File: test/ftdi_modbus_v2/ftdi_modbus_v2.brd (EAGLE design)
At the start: 50 x 50 mm, 31 parts, among them IC1 SP483E, IC2 FT232RL, J1 MB_CONN, J2 CLIFF_DCJACK2.1-2.5MM

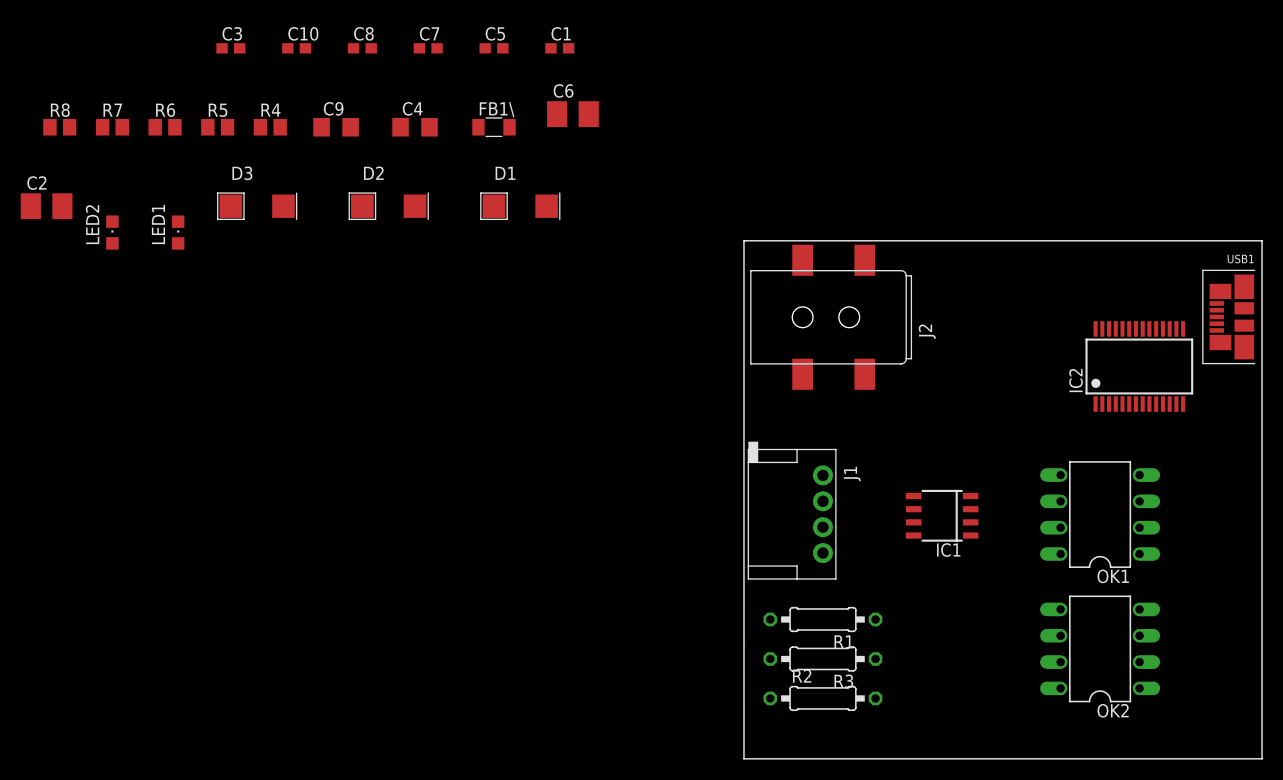
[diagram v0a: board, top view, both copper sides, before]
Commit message: Completed layout of ftdi_rs485_v2 test board. Added more status LEDs
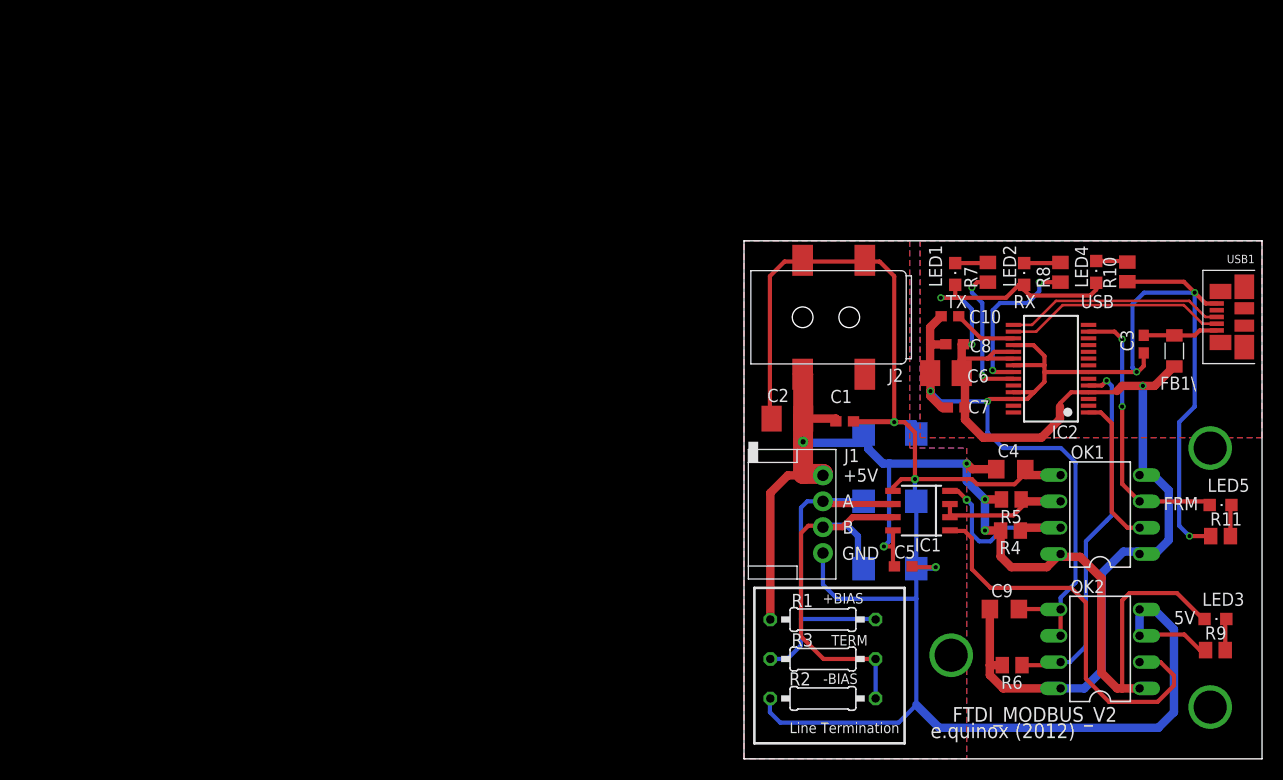
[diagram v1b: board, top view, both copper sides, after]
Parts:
- added LED3, LED4, LED5: AMBER, led:CHIPLED_0805
- added R10, R11, R9: 270, resistor:M0805
- moved R8 97.6 mm to (30.5, 47.0), turned to 90 degrees
- moved R6 96.9 mm to (25.9, 9.04), turned to 180 degrees
- moved C3 92.6 mm to (38.6, 40.0), turned to 270 degrees
- moved LED2 88.1 mm to (27.0, 46.8)
- moved R7 85.7 mm to (23.5, 47.0), turned to 90 degrees
- moved R5 84.6 mm to (25.8, 25.0), turned to 180 degrees
- moved R4 81.4 mm to (25.7, 22.0), turned to 180 degrees
- moved C9 79.5 mm to (25.1, 14.5)
- moved LED1 75.1 mm to (20.4, 46.8)
- moved C2 74.4 mm to (4.19, 32.8)
- moved D3 70.4 mm to (14.1, 18.4), flipped to the bottom, turned to 180 degrees
- moved FB1\ 69.1 mm to (41.5, 39.4), turned to 90 degrees
- moved C10 68.2 mm to (19.9, 42.7), turned to 180 degrees
- moved C4 66.3 mm to (25.8, 28.0)
- moved C8 63.9 mm to (20.3, 40.0), turned to 180 degrees
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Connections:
- new net N$7: LED3.C, R9.2
- new net N$8: LED4.C, R10.2
- new net N$9: LED5.C, R11.2
- net +5V/1: now also LED4.A
- net +5V/2: now also LED3.A
- net FTDI_TXEN: now also LED5.A
- net GND1: now also R10.1, R11.1
- net GND2: now also R9.1
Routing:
- net GND2: track 0.00 -> 181.2 mm, vias 0 -> 3
- net GND1: track 0.00 -> 129.4 mm, vias 0 -> 5
- net +5V/2: track 0.00 -> 123.4 mm, vias 0 -> 5
- net +5V/1: track 0.00 -> 120.9 mm, vias 0 -> 3
- net ISO_RXD: track 0.00 -> 40.2 mm
- net RS485_N: track 0.00 -> 39.2 mm
- net RS485_P: track 0.00 -> 37.2 mm
- net FTDI_RXD: track 0.00 -> 35.7 mm, vias 0 -> 1
- net FTDI_TXEN: track 0.00 -> 27.0 mm, vias 0 -> 2
- net USB_N: track 0.00 -> 21.4 mm
- net USB_P: track 0.00 -> 21.2 mm
- net ISO_TXD: track 0.00 -> 19.0 mm, vias 0 -> 1
- net RX_LED: track 0.00 -> 16.2 mm, vias 0 -> 2
- net FTDI_TXD: track 0.00 -> 14.5 mm
- net TX_LED: track 0.00 -> 14.0 mm, vias 0 -> 2
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- added copper zone on layer 1, net GND1
- added copper zone on layer 16, net GND1
- added copper zone on layer 1, net GND2
- added copper zone on layer 16, net GND2
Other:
- board text added: "+5V"
- board text added: "+BIAS"
- board text added: "-BIAS"
- board text added: "5V"
- board text added: "A"
- board text added: "B"
- board text added: "FRM"
- board text added: "FTDI_MODBUS_V2"
- board text added: "GND"
- board text added: "Line Termination"
- board text added: "RX"
- board text added: "TERM"
- board text added: "TX"
- board text added: "USB"
- board text added: "e.quinox (2012)"
